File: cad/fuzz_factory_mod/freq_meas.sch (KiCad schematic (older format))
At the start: 14 parts, among them U1201 LM2903

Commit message: Continued schematic.
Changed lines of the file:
@@
 $Descr A4 11693 8268
 encoding utf-8
-Sheet 12 22
+Sheet 12 26
 Title ""
 Date ""
@@
 U 1 1 5E6C0D90
 P 2800 2100
-F 0 "U1201" H 2800 2467 50  0000 C CNN
+AR Path="/5DE4AD88/5E6C0B65/5E6C0D90" Ref="U1201"  Part="1"
+AR Path="/5DE4AD88/5EE9EDB4/5E6C0D90" Ref="U1901"  Part="1"
+F 0 "U1901" H 2800 2467 50  0000 C CNN
 F 1 "LM2903" H 2800 2376 50  0000 C CNN
 F 2 "Housings_SOIC:SOIC-8_3.9x4.9mm_Pitch1.27mm" H 2800 2100 50  0001 C CNN
@@
 U 3 1 5E6C2373
 P 6100 1900
-F 0 "U1201" H 6058 1946 50  0000 L CNN
+AR Path="/5DE4AD88/5E6C0B65/5E6C2373" Ref="U1201"  Part="3"
+AR Path="/5DE4AD88/5EE9EDB4/5E6C2373" Ref="U1901"  Part="3"
+F 0 "U1901" H 6058 1946 50  0000 L CNN
 F 1 "LM2903" H 6058 1855 50  0000 L CNN
 F 2 "Housings_SOIC:SOIC-8_3.9x4.9mm_Pitch1.27mm" H 6100 1900 50  0001 C CNN
@@
 U 1 1 5E6C3BDB
 P 3200 1850
-F 0 "R1207" H 3270 1896 50  0000 L CNN
+AR Path="/5DE4AD88/5E6C0B65/5E6C3BDB" Ref="R1207"  Part="1"
+AR Path="/5DE4AD88/5EE9EDB4/5E6C3BDB" Ref="R1915"  Part="1"
+F 0 "R1915" H 3270 1896 50  0000 L CNN
 F 1 "1k" H 3270 1805 50  0000 L CNN
 F 2 "Resistors_SMD:R_0603" V 3130 1850 50  0001 C CNN
@@
 U 1 1 5E6C4D6C
 P 2400 2450
-F 0 "R1205" H 2470 2496 50  0000 L CNN
+AR Path="/5DE4AD88/5E6C0B65/5E6C4D6C" Ref="R1205"  Part="1"
+AR Path="/5DE4AD88/5EE9EDB4/5E6C4D6C" Ref="R1913"  Part="1"
+F 0 "R1913" H 2470 2496 50  0000 L CNN
 F 1 "100k" H 2470 2405 50  0000 L CNN
 F 2 "Resistors_SMD:R_0603" V 2330 2450 50  0001 C CNN
@@
 U 1 1 5E6C5E4F
 P 2100 1750
-F 0 "R1201" H 2170 1796 50  0000 L CNN
+AR Path="/5DE4AD88/5E6C0B65/5E6C5E4F" Ref="R1201"  Part="1"
+AR Path="/5DE4AD88/5EE9EDB4/5E6C5E4F" Ref="R1909"  Part="1"
+F 0 "R1909" H 2170 1796 50  0000 L CNN
 F 1 "4k7" H 2170 1705 50  0000 L CNN
 F 2 "Resistors_SMD:R_0603" V 2030 1750 50  0001 C CNN
@@
 U 1 1 5E6C6A5E
 P 2100 2950
-F 0 "R1202" H 2170 2996 50  0000 L CNN
+AR Path="/5DE4AD88/5E6C0B65/5E6C6A5E" Ref="R1202"  Part="1"
+AR Path="/5DE4AD88/5EE9EDB4/5E6C6A5E" Ref="R1910"  Part="1"
+F 0 "R1910" H 2170 2996 50  0000 L CNN
 F 1 "4k7" H 2170 2905 50  0000 L CNN
 F 2 "Resistors_SMD:R_0603" V 2030 2950 50  0001 C CNN
@@
 U 1 1 5E6C7645
 P 2100 3300
-F 0 "#PWR01202" H 2100 3050 50  0001 C CNN
+AR Path="/5DE4AD88/5E6C0B65/5E6C7645" Ref="#PWR01202"  Part="1"
+AR Path="/5DE4AD88/5EE9EDB4/5E6C7645" Ref="#PWR0195"  Part="1"
+F 0 "#PWR0195" H 2100 3050 50  0001 C CNN
 F 1 "GNDA" H 2105 3127 50  0000 C CNN
 F 2 "" H 2100 3300 50  0001 C CNN
@@
 U 1 1 5E6CBDCF
 P 6000 1400
-F 0 "#PWR01207" H 6000 1250 50  0001 C CNN
+AR Path="/5DE4AD88/5E6C0B65/5E6CBDCF" Ref="#PWR01207"  Part="1"
+AR Path="/5DE4AD88/5EE9EDB4/5E6CBDCF" Ref="#PWR0196"  Part="1"
+F 0 "#PWR0196" H 6000 1250 50  0001 C CNN
 F 1 "+9V" H 6015 1573 50  0000 C CNN
 F 2 "" H 6000 1400 50  0001 C CNN
@@
 U 1 1 5E6CD11C
 P 6000 2300
-F 0 "#PWR01208" H 6000 2050 50  0001 C CNN
+AR Path="/5DE4AD88/5E6C0B65/5E6CD11C" Ref="#PWR01208"  Part="1"
+AR Path="/5DE4AD88/5EE9EDB4/5E6CD11C" Ref="#PWR0197"  Part="1"
+F 0 "#PWR0197" H 6000 2050 50  0001 C CNN
 F 1 "GNDA" H 6005 2127 50  0000 C CNN
 F 2 "" H 6000 2300 50  0001 C CNN
@@
 U 1 1 5E6CDEE4
 P 6250 1500
-F 0 "C1205" V 5998 1500 50  0000 C CNN
+AR Path="/5DE4AD88/5E6C0B65/5E6CDEE4" Ref="C1205"  Part="1"
+AR Path="/5DE4AD88/5EE9EDB4/5E6CDEE4" Ref="C1909"  Part="1"
+F 0 "C1909" V 5998 1500 50  0000 C CNN
 F 1 "100n" V 6089 1500 50  0000 C CNN
 F 2 "Capacitors_SMD:C_0603" H 6288 1350 50  0001 C CNN
@@
 U 1 1 5E6CECB1
 P 6500 1500
-F 0 "#PWR01209" H 6500 1250 50  0001 C CNN
+AR Path="/5DE4AD88/5E6C0B65/5E6CECB1" Ref="#PWR01209"  Part="1"
+AR Path="/5DE4AD88/5EE9EDB4/5E6CECB1" Ref="#PWR0198"  Part="1"
+F 0 "#PWR0198" H 6500 1250 50  0001 C CNN
 F 1 "GNDA" V 6505 1372 50  0000 R CNN
 F 2 "" H 6500 1500 50  0001 C CNN
@@
 U 1 1 5E6CF778
 P 1850 2200
-F 0 "C1203" V 1598 2200 50  0000 C CNN
+AR Path="/5DE4AD88/5E6C0B65/5E6CF778" Ref="C1203"  Part="1"
+AR Path="/5DE4AD88/5EE9EDB4/5E6CF778" Ref="C1907"  Part="1"
+F 0 "C1907" V 1598 2200 50  0000 C CNN
 F 1 "100n" V 1689 2200 50  0000 C CNN
 F 2 "Capacitors_SMD:C_0603" H 1888 2050 50  0001 C CNN
@@
 U 1 1 5E6D0A58
 P 2100 1500
-F 0 "#PWR01201" H 2100 1350 50  0001 C CNN
+AR Path="/5DE4AD88/5E6C0B65/5E6D0A58" Ref="#PWR01201"  Part="1"
+AR Path="/5DE4AD88/5EE9EDB4/5E6D0A58" Ref="#PWR0199"  Part="1"
+F 0 "#PWR0199" H 2100 1350 50  0001 C CNN
 F 1 "+9V" H 2115 1673 50  0000 C CNN
 F 2 "" H 2100 1500 50  0001 C CNN
@@
 U 1 1 5E6D62D7
 P 3200 1600
-F 0 "#PWR01205" H 3200 1450 50  0001 C CNN
+AR Path="/5DE4AD88/5E6C0B65/5E6D62D7" Ref="#PWR01205"  Part="1"
+AR Path="/5DE4AD88/5EE9EDB4/5E6D62D7" Ref="#PWR0200"  Part="1"
+F 0 "#PWR0200" H 3200 1450 50  0001 C CNN
 F 1 "+3.3V" H 3215 1773 50  0000 C CNN
 F 2 "" H 3200 1600 50  0001 C CNN
@@
 U 2 1 5E6DA4DB
 P 2800 5100
-F 0 "U1201" H 2800 5467 50  0000 C CNN
+AR Path="/5DE4AD88/5E6C0B65/5E6DA4DB" Ref="U1201"  Part="2"
+AR Path="/5DE4AD88/5EE9EDB4/5E6DA4DB" Ref="U1901"  Part="2"
+F 0 "U1901" H 2800 5467 50  0000 C CNN
 F 1 "LM2903" H 2800 5376 50  0000 C CNN
 F 2 "Housings_SOIC:SOIC-8_3.9x4.9mm_Pitch1.27mm" H 2800 5100 50  0001 C CNN
@@
 U 1 1 5E6DA4E5
 P 3200 4850
-F 0 "R1208" H 3270 4896 50  0000 L CNN
+AR Path="/5DE4AD88/5E6C0B65/5E6DA4E5" Ref="R1208"  Part="1"
+AR Path="/5DE4AD88/5EE9EDB4/5E6DA4E5" Ref="R1916"  Part="1"
+F 0 "R1916" H 3270 4896 50  0000 L CNN
 F 1 "1k" H 3270 4805 50  0000 L CNN
 F 2 "Resistors_SMD:R_0603" V 3130 4850 50  0001 C CNN
@@
 U 1 1 5E6DA4EF
 P 2400 5450
-F 0 "R1206" H 2470 5496 50  0000 L CNN
+AR Path="/5DE4AD88/5E6C0B65/5E6DA4EF" Ref="R1206"  Part="1"
+AR Path="/5DE4AD88/5EE9EDB4/5E6DA4EF" Ref="R1914"  Part="1"
+F 0 "R1914" H 2470 5496 50  0000 L CNN
 F 1 "100k" H 2470 5405 50  0000 L CNN
 F 2 "Resistors_SMD:R_0603" V 2330 5450 50  0001 C CNN
@@
 U 1 1 5E6DA4F9
 P 2100 4750
-F 0 "R1203" H 2170 4796 50  0000 L CNN
+AR Path="/5DE4AD88/5E6C0B65/5E6DA4F9" Ref="R1203"  Part="1"
+AR Path="/5DE4AD88/5EE9EDB4/5E6DA4F9" Ref="R1911"  Part="1"
+F 0 "R1911" H 2170 4796 50  0000 L CNN
 F 1 "4k7" H 2170 4705 50  0000 L CNN
 F 2 "Resistors_SMD:R_0603" V 2030 4750 50  0001 C CNN
@@
 U 1 1 5E6DA503
 P 2100 5950
-F 0 "R1204" H 2170 5996 50  0000 L CNN
+AR Path="/5DE4AD88/5E6C0B65/5E6DA503" Ref="R1204"  Part="1"
+AR Path="/5DE4AD88/5EE9EDB4/5E6DA503" Ref="R1912"  Part="1"
+F 0 "R1912" H 2170 5996 50  0000 L CNN
 F 1 "4k7" H 2170 5905 50  0000 L CNN
 F 2 "Resistors_SMD:R_0603" V 2030 5950 50  0001 C CNN
@@
 U 1 1 5E6DA50D
 P 2100 6300
-F 0 "#PWR01204" H 2100 6050 50  0001 C CNN
+AR Path="/5DE4AD88/5E6C0B65/5E6DA50D" Ref="#PWR01204"  Part="1"
+AR Path="/5DE4AD88/5EE9EDB4/5E6DA50D" Ref="#PWR0215"  Part="1"
+F 0 "#PWR0215" H 2100 6050 50  0001 C CNN
 F 1 "GNDA" H 2105 6127 50  0000 C CNN
 F 2 "" H 2100 6300 50  0001 C CNN
@@
 U 1 1 5E6DA522
 P 1850 5200
-F 0 "C1204" V 1598 5200 50  0000 C CNN
+AR Path="/5DE4AD88/5E6C0B65/5E6DA522" Ref="C1204"  Part="1"
+AR Path="/5DE4AD88/5EE9EDB4/5E6DA522" Ref="C1908"  Part="1"
+F 0 "C1908" V 1598 5200 50  0000 C CNN
 F 1 "100n" V 1689 5200 50  0000 C CNN
 F 2 "Capacitors_SMD:C_0603" H 1888 5050 50  0001 C CNN
@@
 U 1 1 5E6DA530
 P 2100 4500
-F 0 "#PWR01203" H 2100 4350 50  0001 C CNN
+AR Path="/5DE4AD88/5E6C0B65/5E6DA530" Ref="#PWR01203"  Part="1"
+AR Path="/5DE4AD88/5EE9EDB4/5E6DA530" Ref="#PWR0216"  Part="1"
+F 0 "#PWR0216" H 2100 4350 50  0001 C CNN
 F 1 "+9V" H 2115 4673 50  0000 C CNN
 F 2 "" H 2100 4500 50  0001 C CNN
@@
 U 1 1 5E6DA53C
 P 3200 4600
-F 0 "#PWR01206" H 3200 4450 50  0001 C CNN
+AR Path="/5DE4AD88/5E6C0B65/5E6DA53C" Ref="#PWR01206"  Part="1"
+AR Path="/5DE4AD88/5EE9EDB4/5E6DA53C" Ref="#PWR0217"  Part="1"
+F 0 "#PWR0217" H 3200 4450 50  0001 C CNN
 F 1 "+3.3V" H 3215 4773 50  0000 C CNN
 F 2 "" H 3200 4600 50  0001 C CNN
@@
 U 1 1 5E6F2DED
 P 1800 2950
-F 0 "C1201" V 1548 2950 50  0000 C CNN
+AR Path="/5DE4AD88/5E6C0B65/5E6F2DED" Ref="C1201"  Part="1"
+AR Path="/5DE4AD88/5EE9EDB4/5E6F2DED" Ref="C1905"  Part="1"
+F 0 "C1905" V 1548 2950 50  0000 C CNN
 F 1 "100n" V 1639 2950 50  0000 C CNN
 F 2 "Capacitors_SMD:C_0603" H 1838 2800 50  0001 C CNN
@@
 U 1 1 5E6F6E56
 P 1800 5950
-F 0 "C1202" V 1548 5950 50  0000 C CNN
+AR Path="/5DE4AD88/5E6C0B65/5E6F6E56" Ref="C1202"  Part="1"
+AR Path="/5DE4AD88/5EE9EDB4/5E6F6E56" Ref="C1906"  Part="1"
+F 0 "C1906" V 1548 5950 50  0000 C CNN
 F 1 "100n" V 1639 5950 50  0000 C CNN
 F 2 "Capacitors_SMD:C_0603" H 1838 5800 50  0001 C CNN

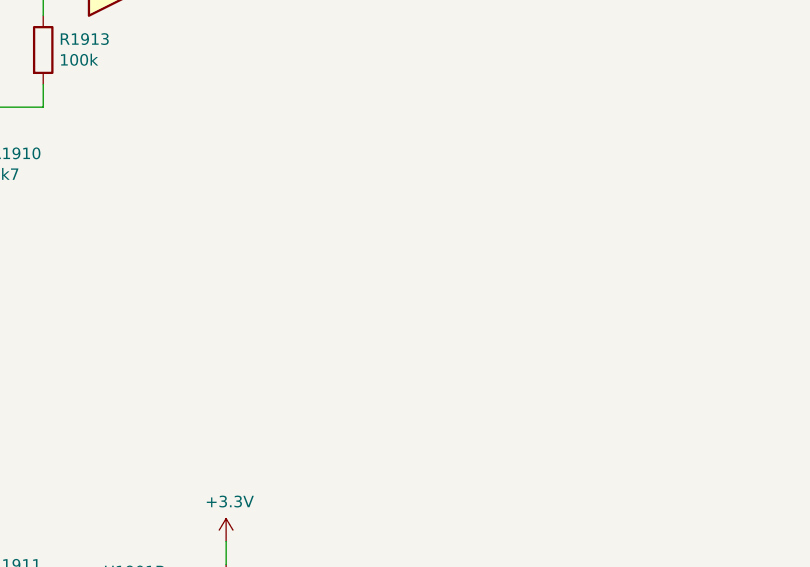
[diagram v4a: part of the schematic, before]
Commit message: Changes architecture.
Corrections on schematic.
Continued Layout placement.
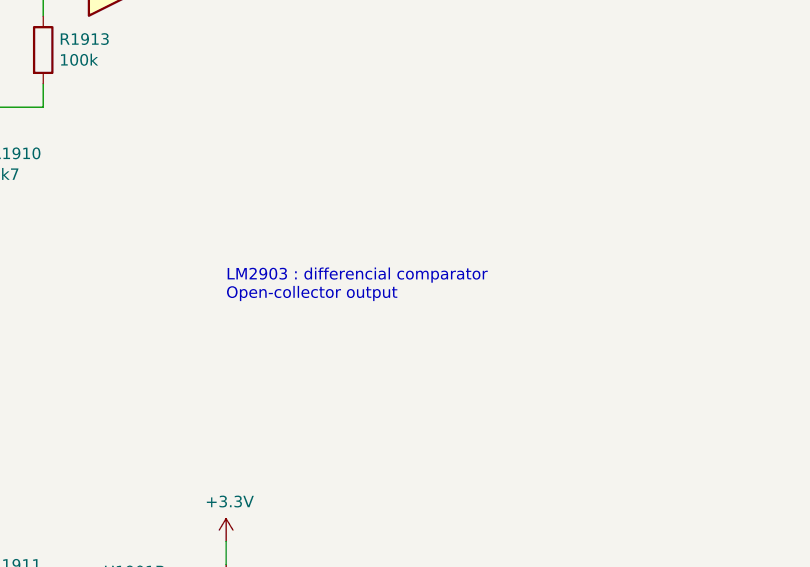
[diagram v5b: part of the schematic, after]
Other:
- note added: "LM2903 : differencial comparator\nOpen-collector output"
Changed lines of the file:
@@
 $Descr A4 11693 8268
 encoding utf-8
-Sheet 20 30
+Sheet 20 22
 Title ""
 Date ""
@@
 Wire Wire Line
 	2100 5600 2100 5000
+Text Notes 3200 3550 0    50   ~ 0
+LM2903 : differencial comparator\nOpen-collector output
 $EndSCHEMATC

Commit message: Continued layout.
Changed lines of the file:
@@
 $Descr A4 11693 8268
 encoding utf-8
-Sheet 20 22
+Sheet 14 22
 Title ""
 Date ""
@@
 AR Path="/5DE4AD88/5E6C0B65/5E6C0D90" Ref="U1201"  Part="1"
 AR Path="/5DE4AD88/5EE9EDB4/5E6C0D90" Ref="U1901"  Part="1"
-F 0 "U1901" H 2800 2467 50  0000 C CNN
+F 0 "U1201" H 2800 2467 50  0000 C CNN
 F 1 "LM2903" H 2800 2376 50  0000 C CNN
 F 2 "Housings_SOIC:SOIC-8_3.9x4.9mm_Pitch1.27mm" H 2800 2100 50  0001 C CNN
@@
 AR Path="/5DE4AD88/5E6C0B65/5E6C2373" Ref="U1201"  Part="3"
 AR Path="/5DE4AD88/5EE9EDB4/5E6C2373" Ref="U1901"  Part="3"
-F 0 "U1901" H 6058 1946 50  0000 L CNN
+F 0 "U1201" H 6058 1946 50  0000 L CNN
 F 1 "LM2903" H 6058 1855 50  0000 L CNN
 F 2 "Housings_SOIC:SOIC-8_3.9x4.9mm_Pitch1.27mm" H 6100 1900 50  0001 C CNN
@@
 AR Path="/5DE4AD88/5E6C0B65/5E6C3BDB" Ref="R1207"  Part="1"
 AR Path="/5DE4AD88/5EE9EDB4/5E6C3BDB" Ref="R1915"  Part="1"
-F 0 "R1915" H 3270 1896 50  0000 L CNN
+F 0 "R1207" H 3270 1896 50  0000 L CNN
 F 1 "1k" H 3270 1805 50  0000 L CNN
 F 2 "Resistors_SMD:R_0603" V 3130 1850 50  0001 C CNN
@@
 AR Path="/5DE4AD88/5E6C0B65/5E6C4D6C" Ref="R1205"  Part="1"
 AR Path="/5DE4AD88/5EE9EDB4/5E6C4D6C" Ref="R1913"  Part="1"
-F 0 "R1913" H 2470 2496 50  0000 L CNN
+F 0 "R1205" H 2470 2496 50  0000 L CNN
 F 1 "100k" H 2470 2405 50  0000 L CNN
 F 2 "Resistors_SMD:R_0603" V 2330 2450 50  0001 C CNN
@@
 AR Path="/5DE4AD88/5E6C0B65/5E6C5E4F" Ref="R1201"  Part="1"
 AR Path="/5DE4AD88/5EE9EDB4/5E6C5E4F" Ref="R1909"  Part="1"
-F 0 "R1909" H 2170 1796 50  0000 L CNN
+F 0 "R1201" H 2170 1796 50  0000 L CNN
 F 1 "4k7" H 2170 1705 50  0000 L CNN
 F 2 "Resistors_SMD:R_0603" V 2030 1750 50  0001 C CNN
@@
 AR Path="/5DE4AD88/5E6C0B65/5E6C6A5E" Ref="R1202"  Part="1"
 AR Path="/5DE4AD88/5EE9EDB4/5E6C6A5E" Ref="R1910"  Part="1"
-F 0 "R1910" H 2170 2996 50  0000 L CNN
+F 0 "R1202" H 2170 2996 50  0000 L CNN
 F 1 "4k7" H 2170 2905 50  0000 L CNN
 F 2 "Resistors_SMD:R_0603" V 2030 2950 50  0001 C CNN
@@
 AR Path="/5DE4AD88/5E6C0B65/5E6C7645" Ref="#PWR01202"  Part="1"
 AR Path="/5DE4AD88/5EE9EDB4/5E6C7645" Ref="#PWR0195"  Part="1"
-F 0 "#PWR0195" H 2100 3050 50  0001 C CNN
+F 0 "#PWR01202" H 2100 3050 50  0001 C CNN
 F 1 "GNDA" H 2105 3127 50  0000 C CNN
 F 2 "" H 2100 3300 50  0001 C CNN
@@
 AR Path="/5DE4AD88/5E6C0B65/5E6CBDCF" Ref="#PWR01207"  Part="1"
 AR Path="/5DE4AD88/5EE9EDB4/5E6CBDCF" Ref="#PWR0196"  Part="1"
-F 0 "#PWR0196" H 6000 1250 50  0001 C CNN
+F 0 "#PWR01207" H 6000 1250 50  0001 C CNN
 F 1 "+9V" H 6015 1573 50  0000 C CNN
 F 2 "" H 6000 1400 50  0001 C CNN
@@
 AR Path="/5DE4AD88/5E6C0B65/5E6CD11C" Ref="#PWR01208"  Part="1"
 AR Path="/5DE4AD88/5EE9EDB4/5E6CD11C" Ref="#PWR0197"  Part="1"
-F 0 "#PWR0197" H 6000 2050 50  0001 C CNN
+F 0 "#PWR01208" H 6000 2050 50  0001 C CNN
 F 1 "GNDA" H 6005 2127 50  0000 C CNN
 F 2 "" H 6000 2300 50  0001 C CNN
@@
 AR Path="/5DE4AD88/5E6C0B65/5E6CDEE4" Ref="C1205"  Part="1"
 AR Path="/5DE4AD88/5EE9EDB4/5E6CDEE4" Ref="C1909"  Part="1"
-F 0 "C1909" V 5998 1500 50  0000 C CNN
+F 0 "C1205" V 5998 1500 50  0000 C CNN
 F 1 "100n" V 6089 1500 50  0000 C CNN
 F 2 "Capacitors_SMD:C_0603" H 6288 1350 50  0001 C CNN
@@
 AR Path="/5DE4AD88/5E6C0B65/5E6CECB1" Ref="#PWR01209"  Part="1"
 AR Path="/5DE4AD88/5EE9EDB4/5E6CECB1" Ref="#PWR0198"  Part="1"
-F 0 "#PWR0198" H 6500 1250 50  0001 C CNN
+F 0 "#PWR01209" H 6500 1250 50  0001 C CNN
 F 1 "GNDA" V 6505 1372 50  0000 R CNN
 F 2 "" H 6500 1500 50  0001 C CNN
@@
 AR Path="/5DE4AD88/5E6C0B65/5E6CF778" Ref="C1203"  Part="1"
 AR Path="/5DE4AD88/5EE9EDB4/5E6CF778" Ref="C1907"  Part="1"
-F 0 "C1907" V 1598 2200 50  0000 C CNN
+F 0 "C1203" V 1598 2200 50  0000 C CNN
 F 1 "100n" V 1689 2200 50  0000 C CNN
 F 2 "Capacitors_SMD:C_0603" H 1888 2050 50  0001 C CNN
@@
 AR Path="/5DE4AD88/5E6C0B65/5E6D0A58" Ref="#PWR01201"  Part="1"
 AR Path="/5DE4AD88/5EE9EDB4/5E6D0A58" Ref="#PWR0199"  Part="1"
-F 0 "#PWR0199" H 2100 1350 50  0001 C CNN
+F 0 "#PWR01201" H 2100 1350 50  0001 C CNN
 F 1 "+9V" H 2115 1673 50  0000 C CNN
 F 2 "" H 2100 1500 50  0001 C CNN
@@
 AR Path="/5DE4AD88/5E6C0B65/5E6D62D7" Ref="#PWR01205"  Part="1"
 AR Path="/5DE4AD88/5EE9EDB4/5E6D62D7" Ref="#PWR0200"  Part="1"
-F 0 "#PWR0200" H 3200 1450 50  0001 C CNN
+F 0 "#PWR01205" H 3200 1450 50  0001 C CNN
 F 1 "+3.3V" H 3215 1773 50  0000 C CNN
 F 2 "" H 3200 1600 50  0001 C CNN
@@
 AR Path="/5DE4AD88/5E6C0B65/5E6DA4DB" Ref="U1201"  Part="2"
 AR Path="/5DE4AD88/5EE9EDB4/5E6DA4DB" Ref="U1901"  Part="2"
-F 0 "U1901" H 2800 5467 50  0000 C CNN
+F 0 "U1201" H 2800 5467 50  0000 C CNN
 F 1 "LM2903" H 2800 5376 50  0000 C CNN
 F 2 "Housings_SOIC:SOIC-8_3.9x4.9mm_Pitch1.27mm" H 2800 5100 50  0001 C CNN
@@
 AR Path="/5DE4AD88/5E6C0B65/5E6DA4E5" Ref="R1208"  Part="1"
 AR Path="/5DE4AD88/5EE9EDB4/5E6DA4E5" Ref="R1916"  Part="1"
-F 0 "R1916" H 3270 4896 50  0000 L CNN
+F 0 "R1208" H 3270 4896 50  0000 L CNN
 F 1 "1k" H 3270 4805 50  0000 L CNN
 F 2 "Resistors_SMD:R_0603" V 3130 4850 50  0001 C CNN
@@
 AR Path="/5DE4AD88/5E6C0B65/5E6DA4EF" Ref="R1206"  Part="1"
 AR Path="/5DE4AD88/5EE9EDB4/5E6DA4EF" Ref="R1914"  Part="1"
-F 0 "R1914" H 2470 5496 50  0000 L CNN
+F 0 "R1206" H 2470 5496 50  0000 L CNN
 F 1 "100k" H 2470 5405 50  0000 L CNN
 F 2 "Resistors_SMD:R_0603" V 2330 5450 50  0001 C CNN
@@
 AR Path="/5DE4AD88/5E6C0B65/5E6DA4F9" Ref="R1203"  Part="1"
 AR Path="/5DE4AD88/5EE9EDB4/5E6DA4F9" Ref="R1911"  Part="1"
-F 0 "R1911" H 2170 4796 50  0000 L CNN
+F 0 "R1203" H 2170 4796 50  0000 L CNN
 F 1 "4k7" H 2170 4705 50  0000 L CNN
 F 2 "Resistors_SMD:R_0603" V 2030 4750 50  0001 C CNN
@@
 AR Path="/5DE4AD88/5E6C0B65/5E6DA503" Ref="R1204"  Part="1"
 AR Path="/5DE4AD88/5EE9EDB4/5E6DA503" Ref="R1912"  Part="1"
-F 0 "R1912" H 2170 5996 50  0000 L CNN
+F 0 "R1204" H 2170 5996 50  0000 L CNN
 F 1 "4k7" H 2170 5905 50  0000 L CNN
 F 2 "Resistors_SMD:R_0603" V 2030 5950 50  0001 C CNN
@@
 AR Path="/5DE4AD88/5E6C0B65/5E6DA50D" Ref="#PWR01204"  Part="1"
 AR Path="/5DE4AD88/5EE9EDB4/5E6DA50D" Ref="#PWR0215"  Part="1"
-F 0 "#PWR0215" H 2100 6050 50  0001 C CNN
+F 0 "#PWR01204" H 2100 6050 50  0001 C CNN
 F 1 "GNDA" H 2105 6127 50  0000 C CNN
 F 2 "" H 2100 6300 50  0001 C CNN
@@
 AR Path="/5DE4AD88/5E6C0B65/5E6DA522" Ref="C1204"  Part="1"
 AR Path="/5DE4AD88/5EE9EDB4/5E6DA522" Ref="C1908"  Part="1"
-F 0 "C1908" V 1598 5200 50  0000 C CNN
+F 0 "C1204" V 1598 5200 50  0000 C CNN
 F 1 "100n" V 1689 5200 50  0000 C CNN
 F 2 "Capacitors_SMD:C_0603" H 1888 5050 50  0001 C CNN
@@
 AR Path="/5DE4AD88/5E6C0B65/5E6DA530" Ref="#PWR01203"  Part="1"
 AR Path="/5DE4AD88/5EE9EDB4/5E6DA530" Ref="#PWR0216"  Part="1"
-F 0 "#PWR0216" H 2100 4350 50  0001 C CNN
+F 0 "#PWR01203" H 2100 4350 50  0001 C CNN
 F 1 "+9V" H 2115 4673 50  0000 C CNN
 F 2 "" H 2100 4500 50  0001 C CNN
@@
 AR Path="/5DE4AD88/5E6C0B65/5E6DA53C" Ref="#PWR01206"  Part="1"
 AR Path="/5DE4AD88/5EE9EDB4/5E6DA53C" Ref="#PWR0217"  Part="1"
-F 0 "#PWR0217" H 3200 4450 50  0001 C CNN
+F 0 "#PWR01206" H 3200 4450 50  0001 C CNN
 F 1 "+3.3V" H 3215 4773 50  0000 C CNN
 F 2 "" H 3200 4600 50  0001 C CNN
@@
 AR Path="/5DE4AD88/5E6C0B65/5E6F2DED" Ref="C1201"  Part="1"
 AR Path="/5DE4AD88/5EE9EDB4/5E6F2DED" Ref="C1905"  Part="1"
-F 0 "C1905" V 1548 2950 50  0000 C CNN
+F 0 "C1201" V 1548 2950 50  0000 C CNN
 F 1 "100n" V 1639 2950 50  0000 C CNN
 F 2 "Capacitors_SMD:C_0603" H 1838 2800 50  0001 C CNN
@@
 AR Path="/5DE4AD88/5E6C0B65/5E6F6E56" Ref="C1202"  Part="1"
 AR Path="/5DE4AD88/5EE9EDB4/5E6F6E56" Ref="C1906"  Part="1"
-F 0 "C1906" V 1548 5950 50  0000 C CNN
+F 0 "C1202" V 1548 5950 50  0000 C CNN
 F 1 "100n" V 1639 5950 50  0000 C CNN
 F 2 "Capacitors_SMD:C_0603" H 1838 5800 50  0001 C CNN
